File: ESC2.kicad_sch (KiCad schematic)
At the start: 35 parts, among them J7 MOTOR_A, J8 MOTOR_B, J9 MOTOR_C, Q10 Q_NMOS_GDS, Q11 Q_NMOS_GDS, Q12 Q_NMOS_GDS, Q13 Q_NMOS_GDS, Q8 Q_NMOS_GDS, Q9 Q_NMOS_GDS, U15 DRV8300D, U7 STM32G071GBUxN

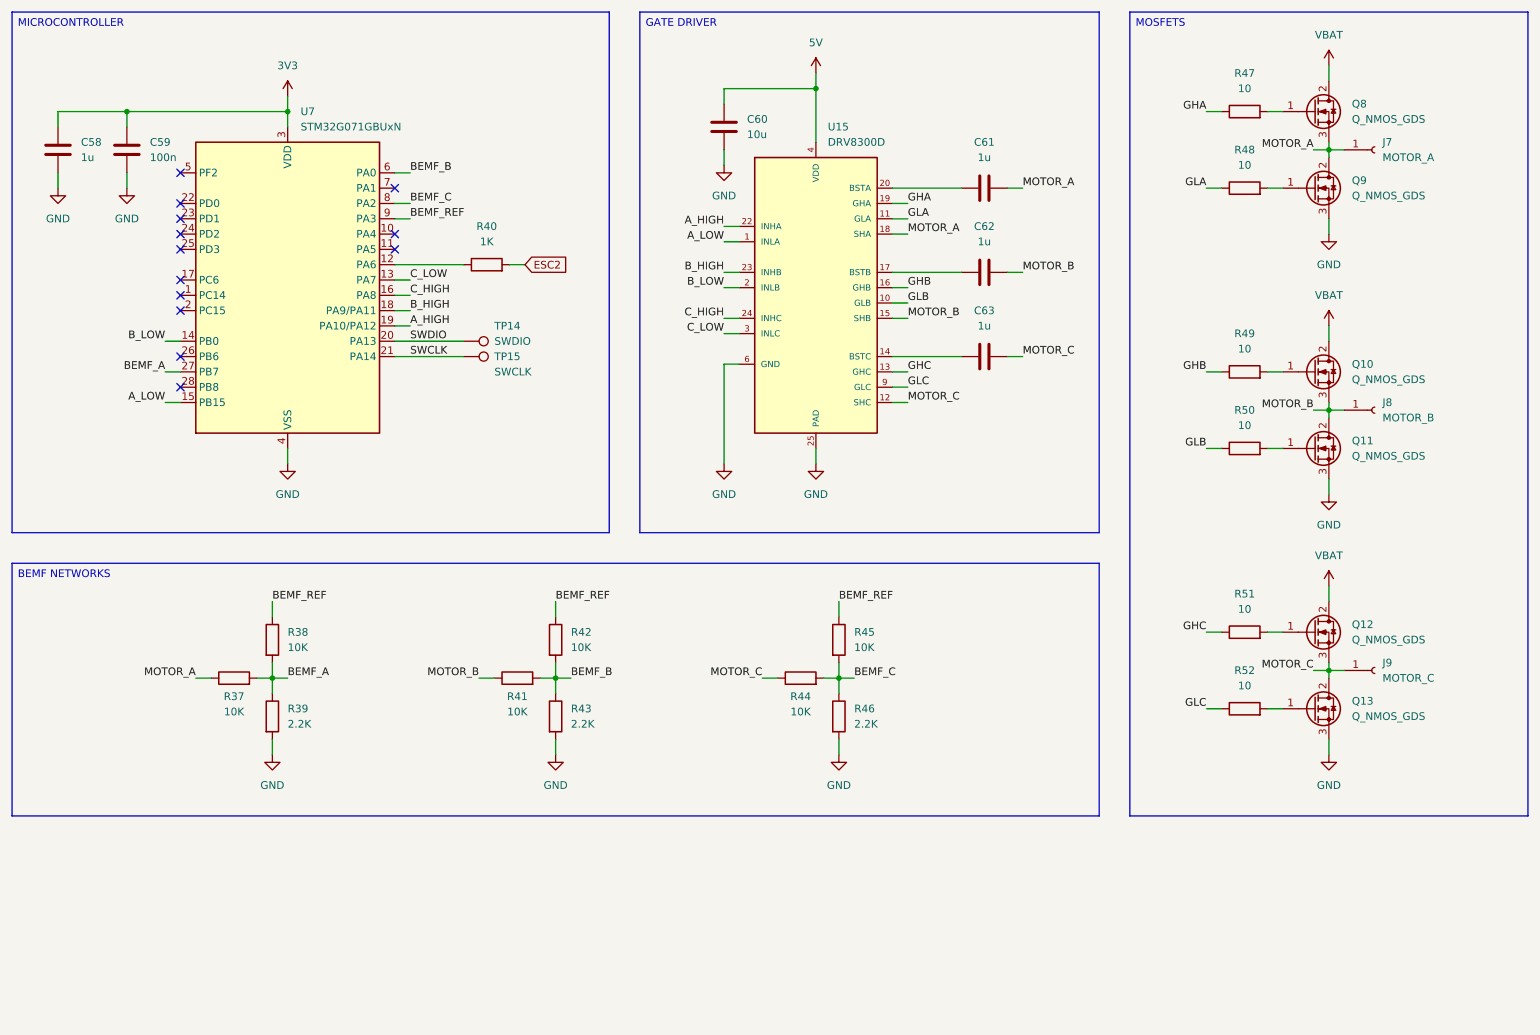
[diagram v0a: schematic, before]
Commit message: Footprints and revision
Added the missing footprints.
Updated a all the schematics.
Completed an initial review of the schematics.

TODO:
Perform a deep review of the schematics before committing to layout.
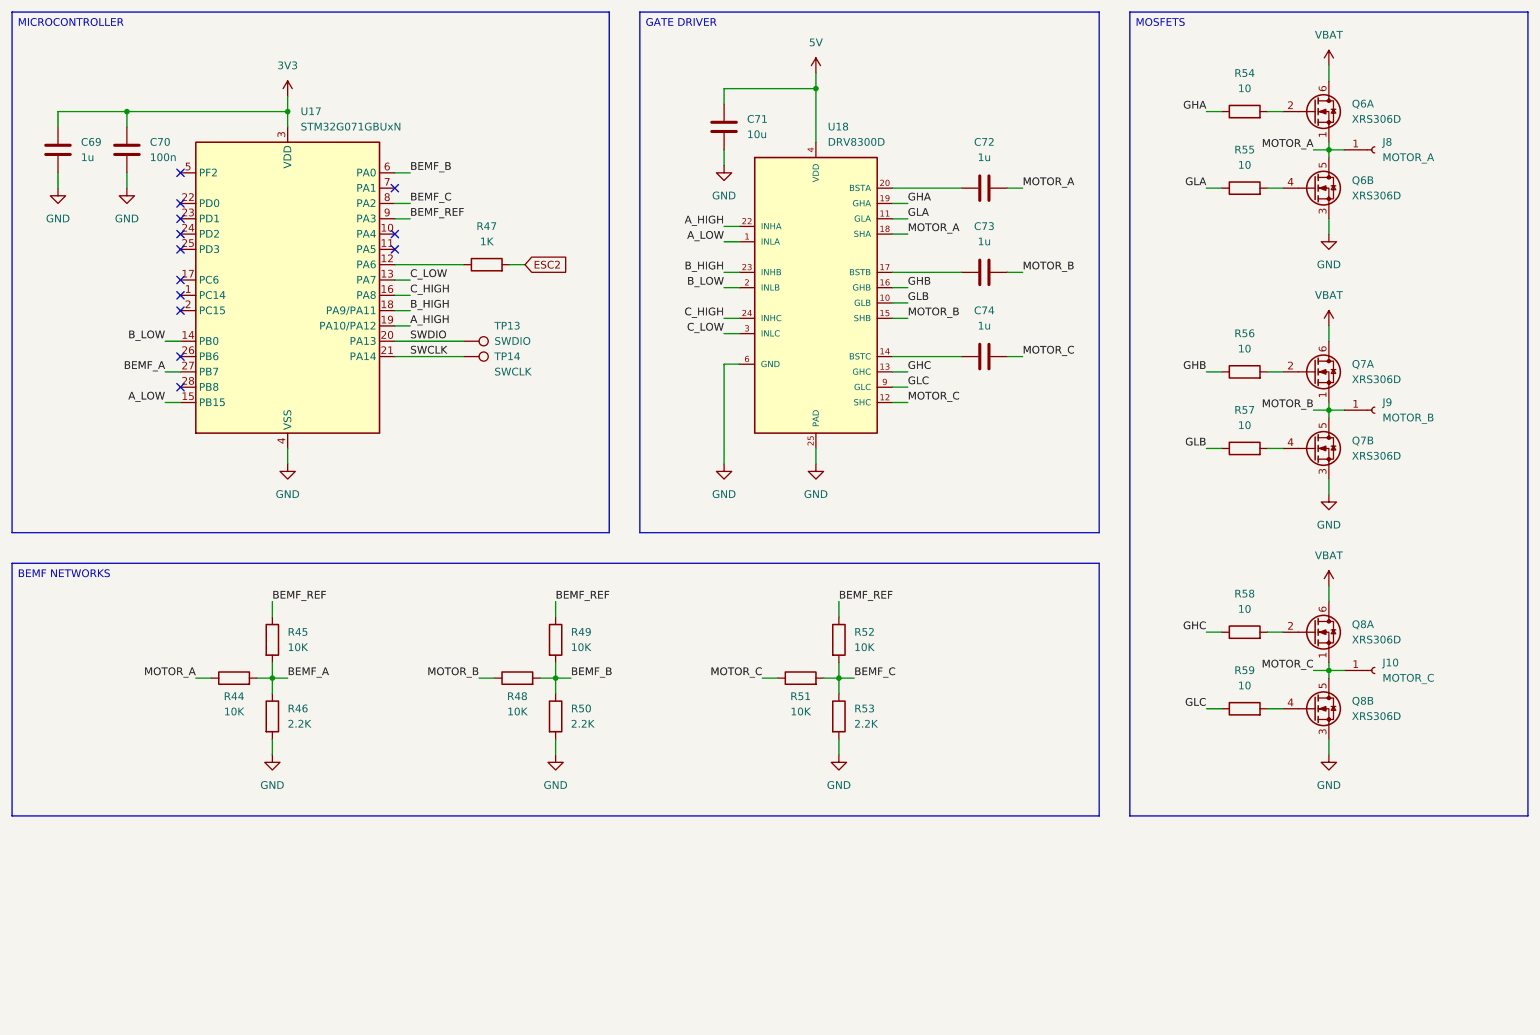
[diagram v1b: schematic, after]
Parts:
- removed Q10, Q11, Q12, Q13, Q8, Q9: Q_NMOS_GDS, symbol Transistor_FET:Q_NMOS_GDS
- added Q6, Q7, Q8: XRS306D, Custom_Parts:PDFN8, symbol Transistor_FET:Q_Dual_NMOS_S1G1S2G2D2D1
- C69: renamed from C58; footprint (none) -> Capacitor_SMD:C_0603_1608Metric
- C70: renamed from C59; footprint (none) -> Capacitor_SMD:C_0603_1608Metric
- C71: renamed from C60; footprint (none) -> Capacitor_SMD:C_0805_2012Metric
- C72: renamed from C61; footprint (none) -> Capacitor_SMD:C_0603_1608Metric
- C73: renamed from C62; footprint (none) -> Capacitor_SMD:C_0603_1608Metric
- C74: renamed from C63; footprint (none) -> Capacitor_SMD:C_0603_1608Metric
- R44: renamed from R37; footprint (none) -> Resistor_SMD:R_0603_1608Metric
- R45: renamed from R38; footprint (none) -> Resistor_SMD:R_0603_1608Metric
- R46: renamed from R39; footprint (none) -> Resistor_SMD:R_0603_1608Metric
- R47: renamed from R40; footprint (none) -> Resistor_SMD:R_0603_1608Metric
- R48: renamed from R41; footprint (none) -> Resistor_SMD:R_0603_1608Metric
- R49: renamed from R42; footprint (none) -> Resistor_SMD:R_0603_1608Metric
- R50: renamed from R43; footprint (none) -> Resistor_SMD:R_0603_1608Metric
- R51: renamed from R44; footprint (none) -> Resistor_SMD:R_0603_1608Metric
- R52: renamed from R45; footprint (none) -> Resistor_SMD:R_0603_1608Metric
- R53: renamed from R46; footprint (none) -> Resistor_SMD:R_0603_1608Metric
- R54: renamed from R47; footprint (none) -> Resistor_SMD:R_0603_1608Metric
- R55: renamed from R48; footprint (none) -> Resistor_SMD:R_0603_1608Metric
- R56: renamed from R49; footprint (none) -> Resistor_SMD:R_0603_1608Metric
- R57: renamed from R50; footprint (none) -> Resistor_SMD:R_0603_1608Metric
- R58: renamed from R51; footprint (none) -> Resistor_SMD:R_0603_1608Metric
- R59: renamed from R52; footprint (none) -> Resistor_SMD:R_0603_1608Metric
- renumbered J9 to J10, J7 to J8, J8 to J9, TP14 to TP13, TP15 to TP14, U7 to U17, U15 to U18
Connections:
- net GND: now also Q6.3 (S), Q7.3 (S), Q8.3 (S)
- net MOTOR_A: now also Q6.1 (S), Q6.5 (D)
- net MOTOR_B: now also Q7.1 (S), Q7.5 (D)
- net MOTOR_C: now also Q8.1 (S), Q8.5 (D)
- net VBAT: now also Q6.6 (D), Q7.6 (D), Q8.6 (D)
- net at R58.2: now also Q8.2 (G)
- net at R59.2: now also Q8.4 (G)
- net at R57.2: now also Q7.4 (G)
- net at R54.2: now also Q6.2 (G)
- net at R56.2: now also Q7.2 (G)
- net at R55.2: now also Q6.4 (G)

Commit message: ESC design
Updated the ESC schematics.
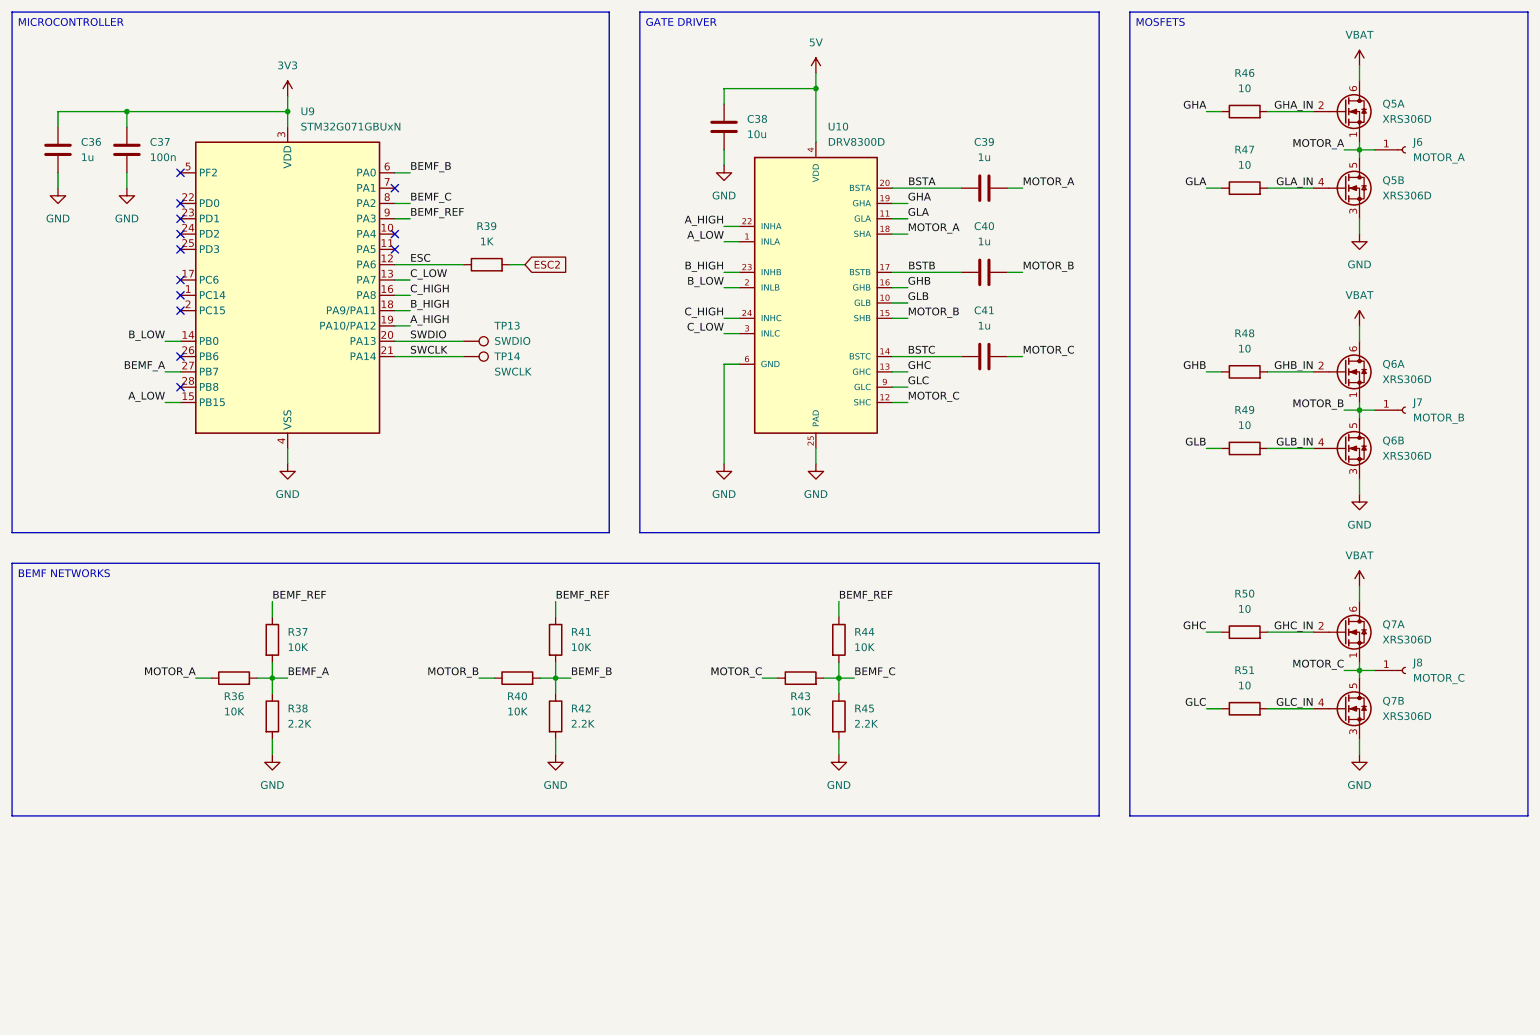
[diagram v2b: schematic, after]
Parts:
- renumbered C69 to C36, C70 to C37, C71 to C38, C72 to C39, C73 to C40, C74 to C41, J8 to J6, J9 to J7, J10 to J8, Q6 to Q5, Q7 to Q6, Q8 to Q7, R44 to R36, R45 to R37, R46 to R38, R47 to R39, R48 to R40, R49 to R41, R50 to R42, R51 to R43, R52 to R44, R53 to R45, R54 to R46, R55 to R47, R56 to R48, R57 to R49, R58 to R50, R59 to R51, U18 to U10, U17 to U9
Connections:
- net GLB_IN: now reaches Q6.4 (G), R49.2
- net ESC: now reaches R39.1, U9.12 (PA6)
- net GHC_IN: now reaches Q7.2 (G), R50.2
- net BSTC: now reaches C41.1, U10.14 (BSTC)
- net BSTB: now reaches C40.1, U10.17 (BSTB)
- net BSTA: now reaches C39.1, U10.20 (BSTA)
- net GLC_IN: now reaches Q7.4 (G), R51.2
- net GHB_IN: now reaches Q6.2 (G), R48.2
- net GHA_IN: now reaches Q5.2 (G), R46.2
- net GLA_IN: now reaches Q5.4 (G), R47.2
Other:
- company: (none) -> DavidMolTor
- title: (none) -> THUNDER HORSE
- moved on the sheet: J6, J7, J8, Q5A, Q5B, Q6A, Q6B, Q7A, Q7B

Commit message: Connectors and tag
Added bulk capacitance for each ESC.
Added SWD connector.
Updated all tags.

TODO:
Add pads for the unconnected GPIO pins.
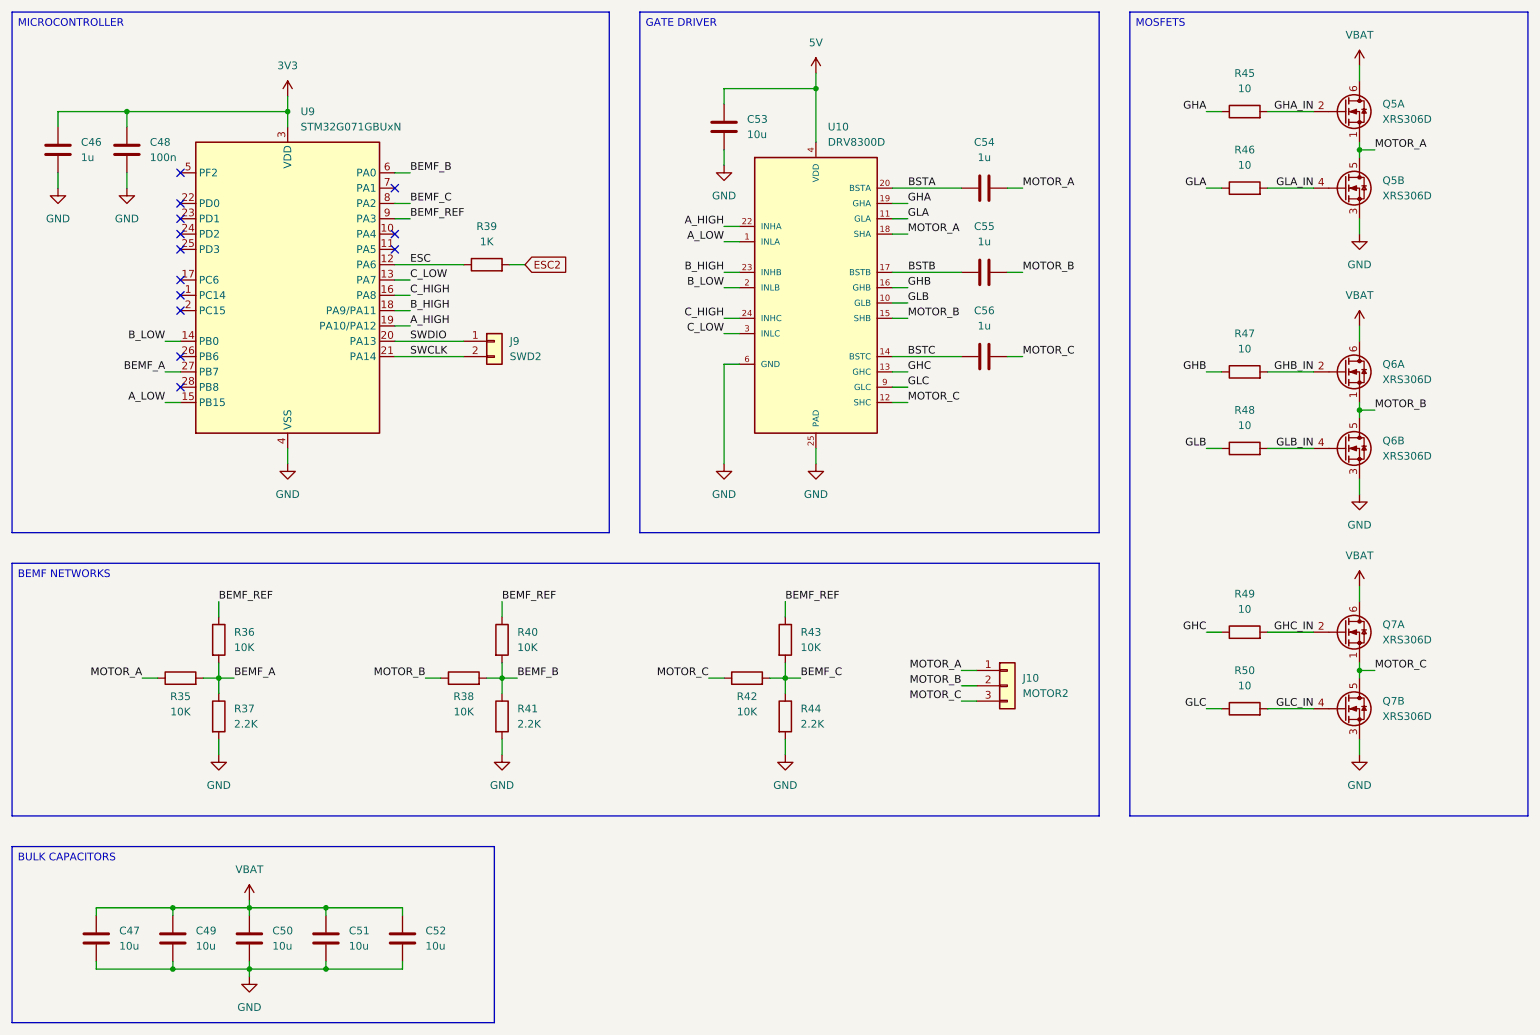
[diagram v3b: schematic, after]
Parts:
- removed J6: MOTOR_A, TestPoint:TestPoint_Pad_D2.0mm, symbol Connector:Conn_01x01_Socket
- removed J7: MOTOR_B, TestPoint:TestPoint_Pad_D2.0mm, symbol Connector:Conn_01x01_Socket
- removed J8: MOTOR_C, TestPoint:TestPoint_Pad_D2.0mm, symbol Connector:Conn_01x01_Socket
- removed R45: 2.2K, Resistor_SMD:R_0603_1608Metric, symbol Device:R
- removed TP13: SWDIO, TestPoint:TestPoint_Pad_D1.0mm, symbol Connector:TestPoint
- removed TP14: SWCLK, TestPoint:TestPoint_Pad_D1.0mm, symbol Connector:TestPoint
- added C47, C49, C50, C51, C52: 10u, symbol Device:C
- added J10: MOTOR2, Custom_Parts:PAD_3_SQUARE_SOLID_2.0x2.0mm_P2.5mm, symbol Connector_Generic:Conn_01x03
- added J9: SWD2, symbol Connector_Generic:Conn_01x02
- added R35: 10K, Resistor_SMD:R_0603_1608Metric, symbol Device:R
- R37, R41, R44: value 10K -> 2.2K
- R38, R42: value 2.2K -> 10K
- renumbered C36 to C46, C37 to C48, C38 to C53, C39 to C54, C40 to C55, C41 to C56, R46 to R45, R47 to R46, R48 to R47, R49 to R48, R50 to R49, R51 to R50
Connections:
- net BEMF_A: now also R37.1, R35.2; no longer R37.2, R38.1
- net BEMF_B: now also R38.2, R41.1; no longer R41.2, R42.1
- net BEMF_C: now also R42.2, R44.1; no longer R44.2
- net BEMF_REF: now also R36.1, R40.1, R43.1; no longer R37.1, R41.1, R44.1
- net GND: now also R37.2, R41.2, R44.2, C47.2, C49.2, C50.2, C51.2, C52.2; no longer R38.2, R42.2
- net MOTOR_A: now also J10.1 (Pin_1), R35.1; no longer R36.1
- net MOTOR_B: now also R38.1, J10.2 (Pin_2); no longer R40.1
- net MOTOR_C: now also R42.1, J10.3 (Pin_3); no longer R43.1
- net SWCLK: now also J9.2 (Pin_2)
- net SWDIO: now also J9.1 (Pin_1)
- net VBAT: now also C47.1, C49.1, C50.1, C51.1, C52.1
